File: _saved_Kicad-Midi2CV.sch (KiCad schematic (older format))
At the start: 70 parts, among them IC1 MCP4725module, IC2 MCP4725module, J1 Doepfer connector, J10 CV4, J11 Gate1, J12 GateConn, J13 Gate2, J14 Gate3, J15 Gate4, J16 I2C_Conn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

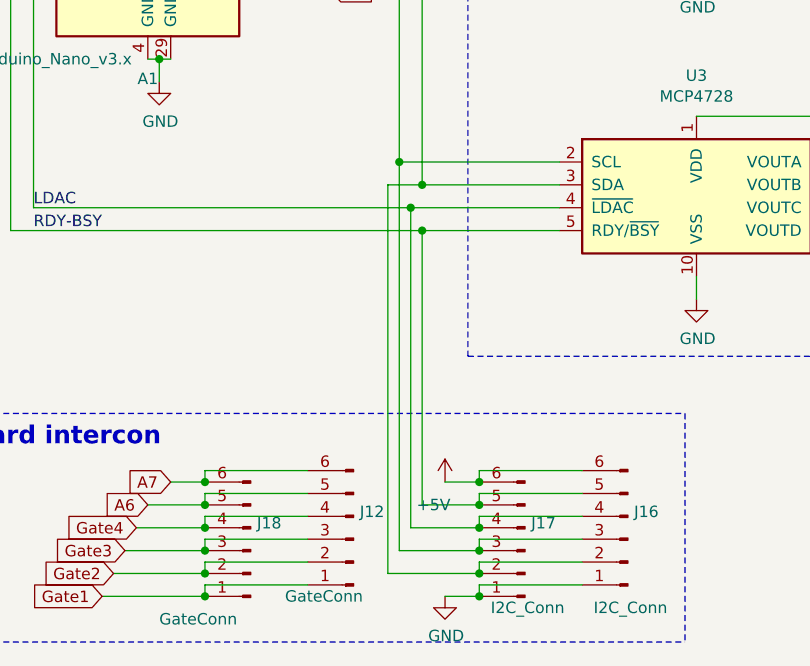
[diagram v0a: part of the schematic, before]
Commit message: Update _saved_Kicad-Midi2CV.sch
Swap SCL and SDA in  board interconnector
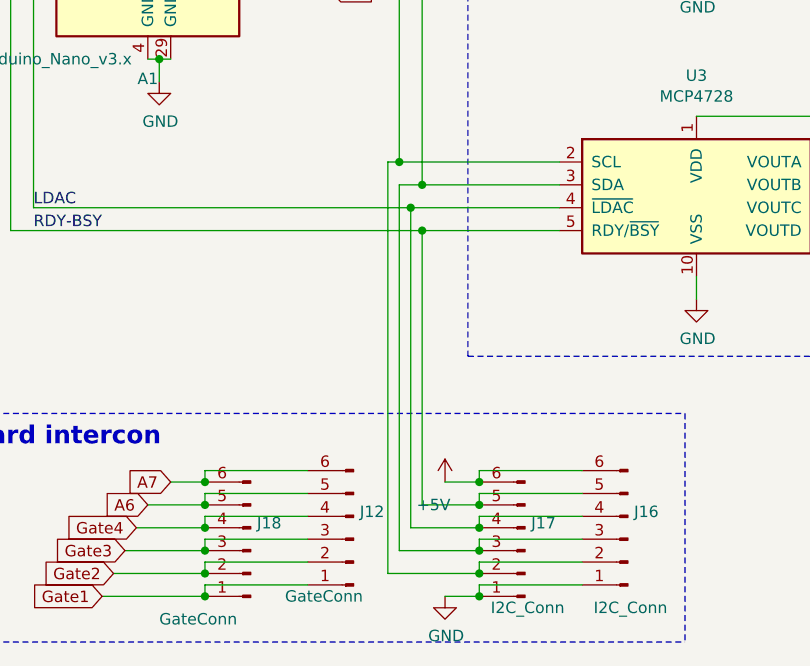
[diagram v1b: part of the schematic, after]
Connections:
- wire segments 320 -> 321
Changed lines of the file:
@@
 Wire Wire Line
 	6000 7350 5650 7350
-Wire Wire Line
-	5650 7350 5650 5650
 Connection ~ 6000 7350
-Connection ~ 5650 5650
-Wire Wire Line
-	5750 5750 5600 5750
-Wire Wire Line
-	5600 5750 5600 7450
-Connection ~ 5750 5750
 Wire Wire Line
 	5600 7450 6000 7450
@@
 Text Label 4650 1600 0    50   ~ 0
 -12v
+Wire Wire Line
+	5600 5650 5650 5650
+Wire Wire Line
+	5600 5650 5600 7450
+Connection ~ 5650 5650
+Wire Wire Line
+	5750 5750 5650 5750
+Wire Wire Line
+	5650 5750 5650 7350
+Connection ~ 5750 5750
 $EndSCHEMATC

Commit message: Analogue card routed - no GND
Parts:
- added J19: CV7 in, Connector_Audio:AudioJack3StereoNarrow-PJ-321, symbol Connector:AudioJack2
- added J20: CV3 in, Connector_Audio:AudioJack3StereoNarrow-PJ-321, symbol Connector:AudioJack2
- added R25, R26, R27, R28: 10k, Resistor_SMD:R_0805_2012Metric_Pad1.15x1.40mm_HandSolder, symbol Device:R
- C8: value C -> 100n
- J4: value CV in -> CV6 in
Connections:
- net labels added: Vout1, Vout2
- wire segments 321 -> 341
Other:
- moved on the sheet: J4, J6, J7, J9, R10, R8

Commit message: AJ-SO8
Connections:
- wire segments 341 -> 340
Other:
- moved on the sheet: J10, J11, J13, J14, J15, J19, J20, J4, J6, J7, J9, R10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
